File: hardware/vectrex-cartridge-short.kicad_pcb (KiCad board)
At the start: 2 copper layers, 48 x 66.1 mm, 18 parts, among them CON1 vectrex-edge-connector, SW2 SW_DIP_x03, U1 AT27C256R-70PU / AT27C512R-70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, U2 DS2431+ TO-92

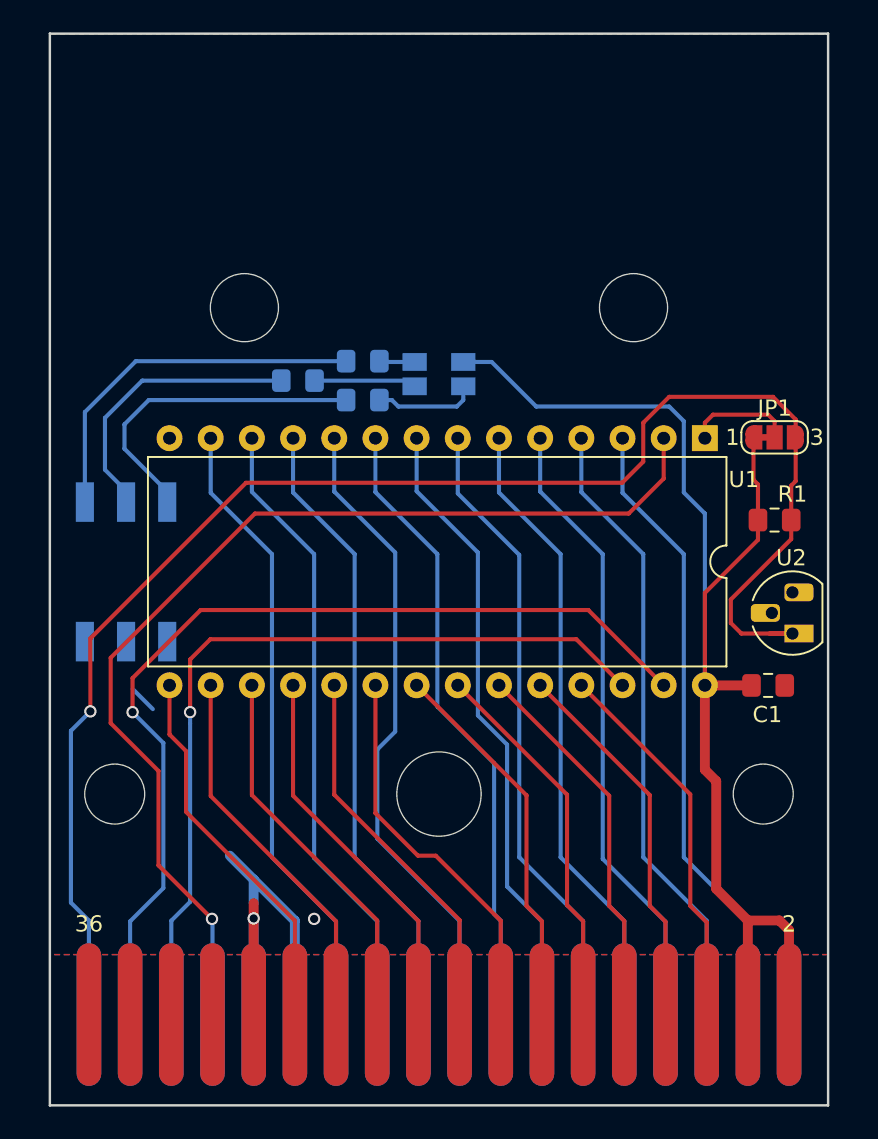
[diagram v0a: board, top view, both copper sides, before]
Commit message: added RGB LED to Vectrex Cartridge v1.1, also added stand-alone LED PCB v1.0
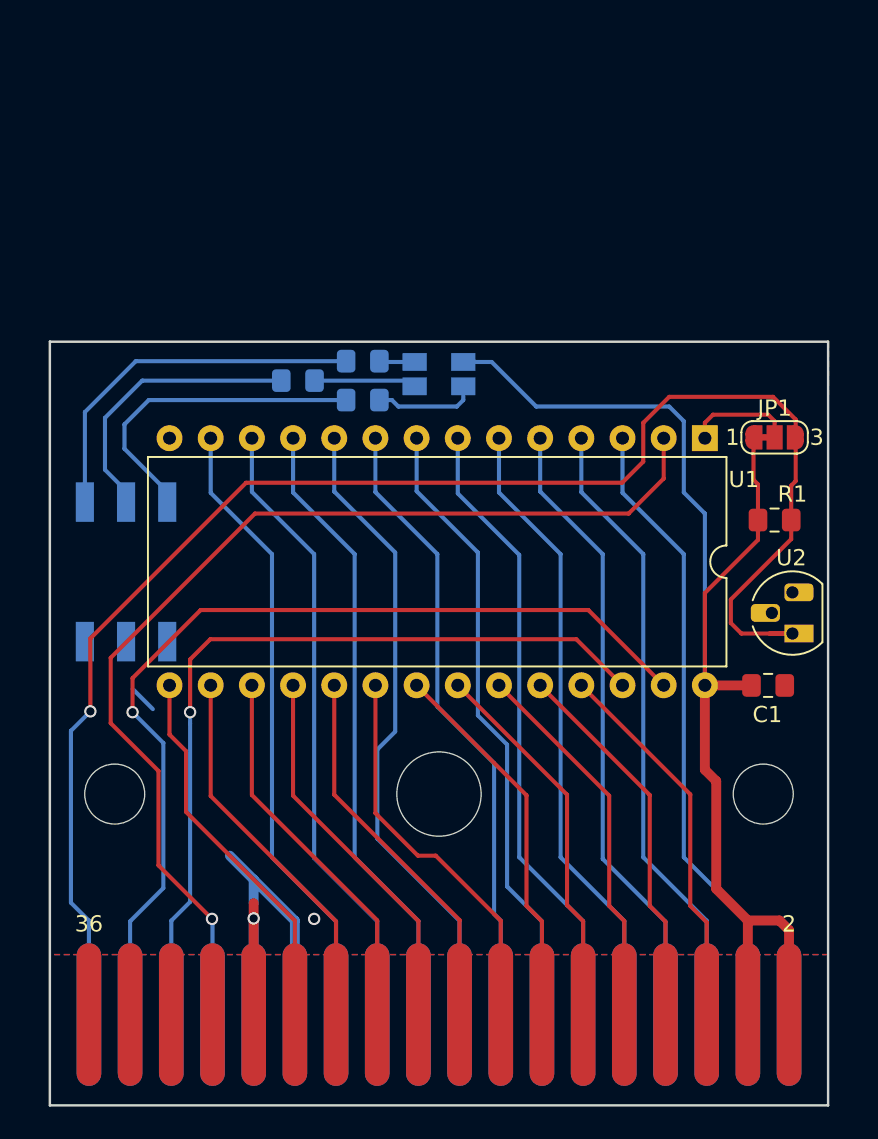
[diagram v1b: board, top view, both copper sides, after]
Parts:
- removed G3: LOGO, vectrex-cartridge:vectrex-uk-soldermask
- removed H4, H5: 4.2mm, vectrex-cartridge:Mounting_Hole_D4.2mm
- G1: footprint vectrex-cartridge:vectrex-us-soldermask -> vectrex-cartridge:vectrex-us-soldermask-37mm; moved to B.Cu
- moved G1 24.5 mm to (146.1, 101.9), turned to 180 degrees
- renumbered SW2 to SW1
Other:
- board size 48 x 66.1 mm -> 48 x 47.1 mm
- board text removed: "4.2mm hole"

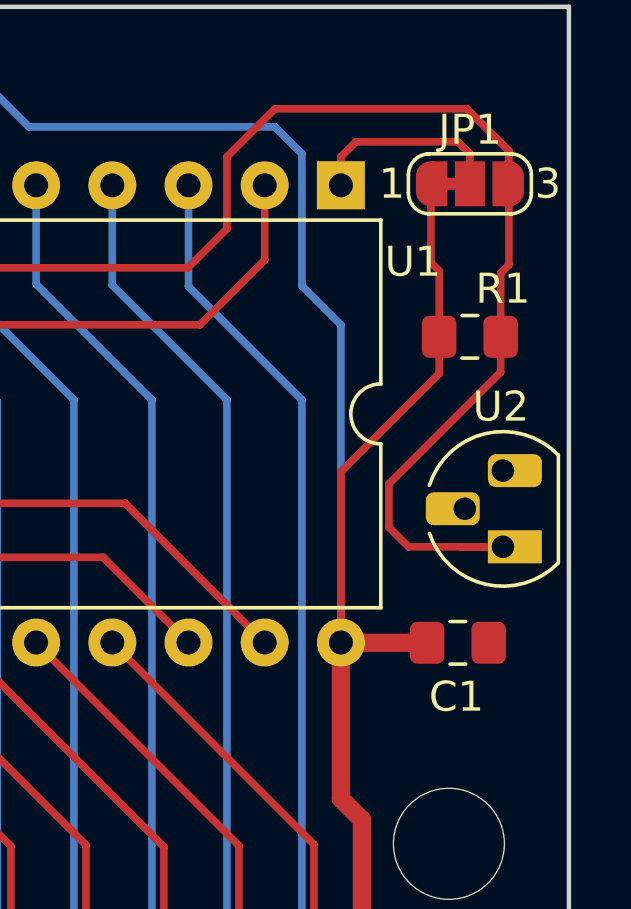
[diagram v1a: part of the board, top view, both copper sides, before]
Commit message: Updated DS2431 footprint, and many little tweaks for v1.2
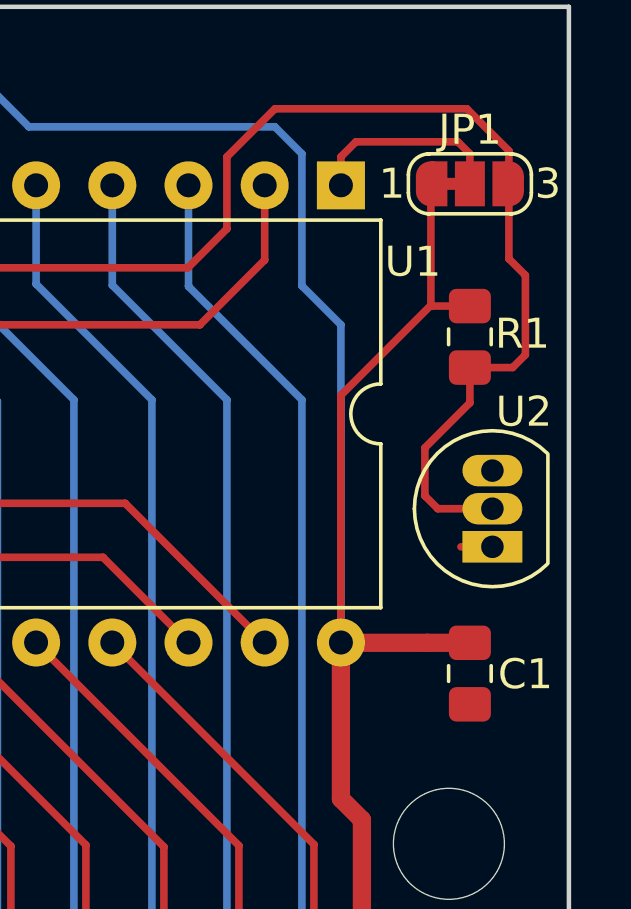
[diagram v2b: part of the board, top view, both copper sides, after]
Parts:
- added G2: LOGO, vectrex-cartridge:vectrex-us-soldermask-15mm, F.Cu at (141.7, 92.2)
- R2, R3: value 220 0805 -> 200 0805
- R4: value 150 0805 -> 120 0805
- U2: footprint vectrex-cartridge:TO-92L_HandSolder -> vectrex-cartridge:TO-92_Inline_BW
- moved C1 1.10 mm to (162.4, 111.9), turned to 270 degrees
- moved U2 0.35 mm to (163.2, 107.7)
- turned R1 to 270 degrees
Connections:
- U2 pad 1: V-PB6 -> GND
- U2 pad 2: GND -> V-PB6
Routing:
- net V-PB6: track 95.2 -> 92.2 mm
- net +5V: track 81.0 -> 83.5 mm
- net GND: track 27.5 -> 28.6 mm

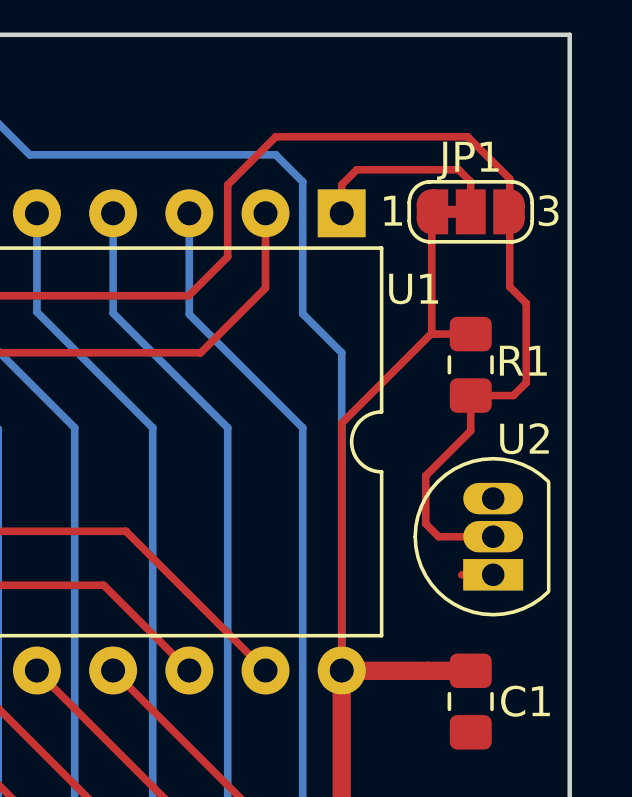
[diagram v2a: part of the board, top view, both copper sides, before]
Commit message: migrate 3D shapes to built-in KiCad 6.x location
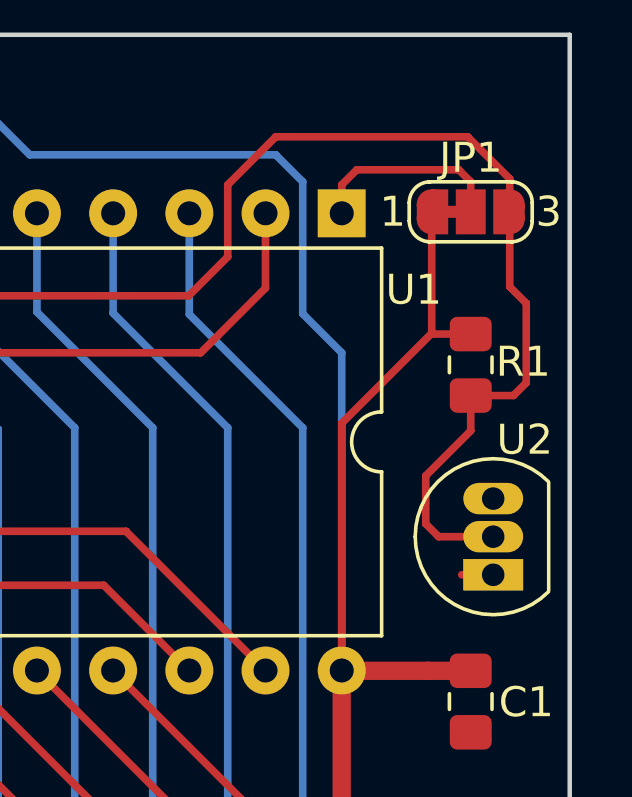
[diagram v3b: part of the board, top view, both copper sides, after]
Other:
- net class Default removed
- net class Large removed

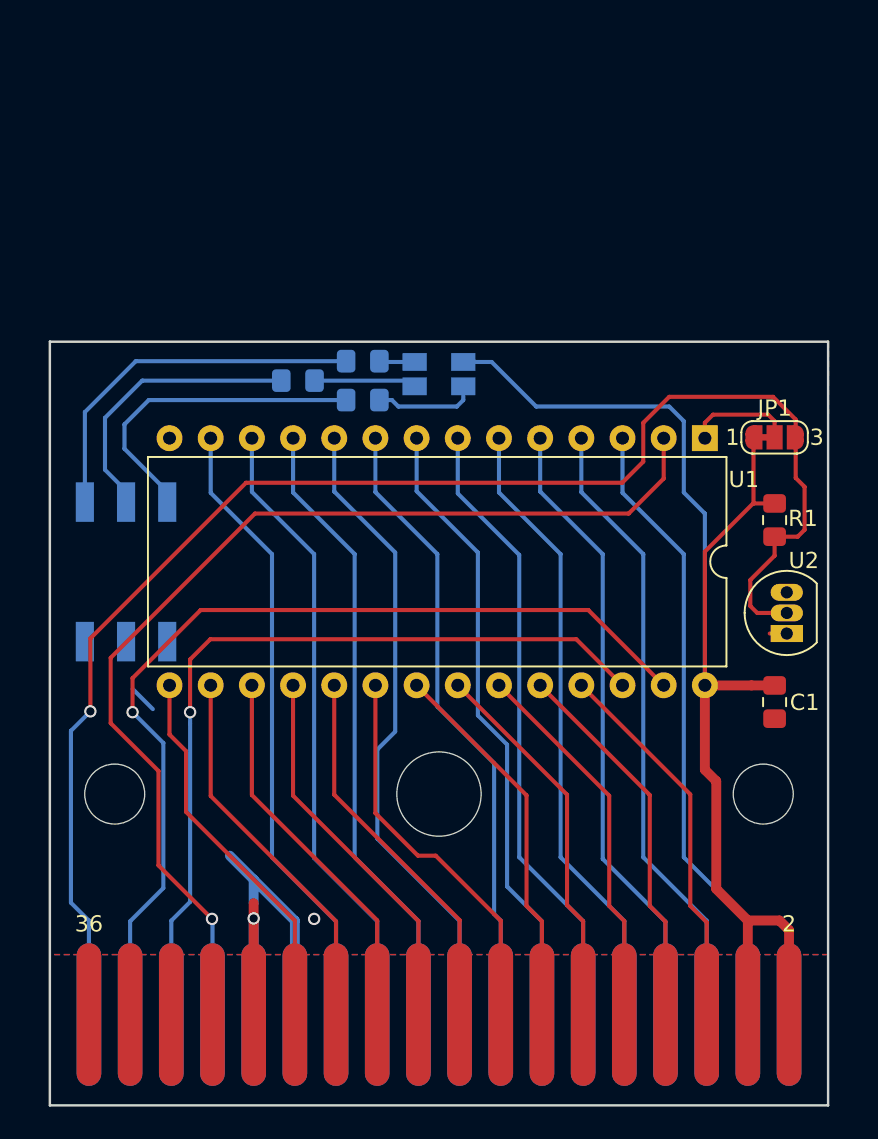
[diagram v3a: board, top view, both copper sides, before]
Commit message: update vectrex-cartridge-short to v1.4 all SMT
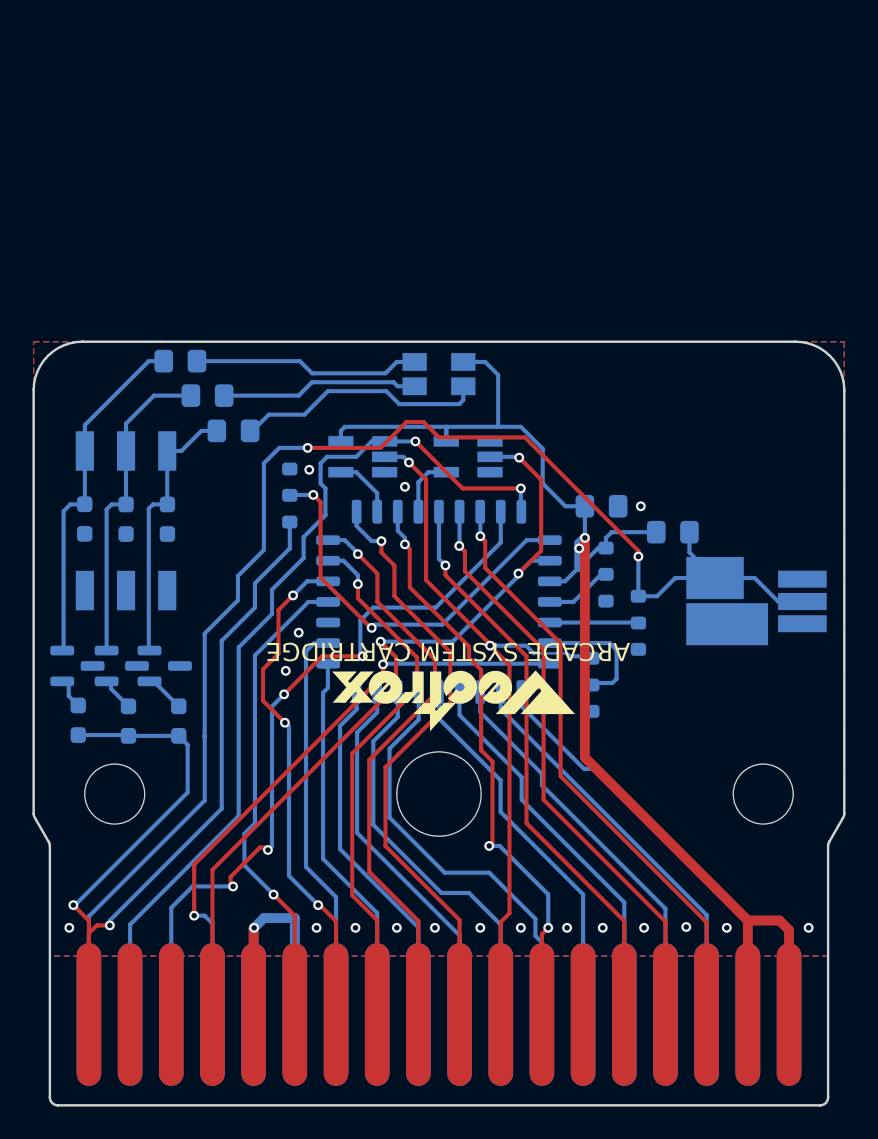
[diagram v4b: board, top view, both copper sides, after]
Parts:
- added JP2: PB6/A16/GND, vectrex-cartridge:R_0603_1608Metric_Jumper_12_Bridged, B.Cu at (154.0, 106.2)
- added JP3: IRQ/A17/GND, vectrex-cartridge:R_0603_1608Metric_Jumper_12_Bridged, B.Cu at (132.5, 100.0)
- added JP4: GND/A18/+5V, vectrex-cartridge:R_0603_1608Metric_Jumper_12_Bridged, B.Cu at (152.0, 104.9)
- added Q2: MMBT4403, Package_TO_SOT_SMD:SOT-23, B.Cu at (124.8, 109.7)
- added Q3: MMBT4403, Package_TO_SOT_SMD:SOT-23, B.Cu at (122.1, 109.7)
- added Q4: MMBT4403, Package_TO_SOT_SMD:SOT-23, B.Cu at (119.4, 109.7)
- added R12: 0 0603, Resistor_SMD:R_0603_1608Metric_Pad0.98x0.95mm_HandSolder, B.Cu at (125.0, 100.7)
- added R13: 0 0603, Resistor_SMD:R_0603_1608Metric_Pad0.98x0.95mm_HandSolder, B.Cu at (122.4, 100.7)
- added R14: 0 0603, Resistor_SMD:R_0603_1608Metric_Pad0.98x0.95mm_HandSolder, B.Cu at (119.8, 100.6)
- added R22: 1k 0603, Resistor_SMD:R_0603_1608Metric_Pad0.98x0.95mm_HandSolder, B.Cu at (125.7, 113.1)
- added R23: 1k 0603, Resistor_SMD:R_0603_1608Metric_Pad0.98x0.95mm_HandSolder, B.Cu at (122.5, 113.1)
- added R24: 1k 0603, Resistor_SMD:R_0603_1608Metric_Pad0.98x0.95mm_HandSolder, B.Cu at (119.5, 113.0)
- added U3: SN74AHC1G04DBVR (Schmitt-Trigger), Package_TO_SOT_SMD:SOT-23-5_HandSoldering, B.Cu at (143.5, 96.8)
- added U4: DS2431+ TO-92, vectrex-cartridge:TO-92_Inline_BW_SMT, B.Cu at (164.1, 107.0)
- added U5: DS2431G+ 2-SFN, vectrex-cartridge:2SFN_6mmx6mm, B.Cu at (159.2, 105.7)
- C1, R1: moved to B.Cu
- CON1: footprint vectrex-cartridge:vectrex-edge-connector-thinner-no-soldermask -> vectrex-cartridge:vectrex-edge-connector-thinner-no-soldermask-no-silk
- G1: footprint vectrex-cartridge:vectrex-us-soldermask-37mm -> vectrex-cartridge:vectrex-us-soldermask-15mm
- G2: footprint vectrex-cartridge:vectrex-us-soldermask-15mm -> vectrex-cartridge:vectrex-us-silkscreen-15mm
- JP1: value SolderJumper_3_Bridged12 -> C_A15/A15/GND; footprint vectrex-cartridge:SolderJumper-3_P1.3mm_Bridged12_RoundedPad1.0x1.5mm_NumberLabels -> vectrex-cartridge:R_0603_1608Metric_Jumper_12_Bridged; moved to B.Cu
- R2, R3: value 200 0805 -> 150 0805
- R4: value 120 0805 -> 200 0805
- SW1: footprint Button_Switch_SMD:SW_DIP_SPSTx03_Slide_6.7x9.18mm_W8.61mm_P2.54mm_LowProfile -> vectrex-cartridge:SW_DIP_SPSTx03_Slide_6.7x9.18mm_W8.61mm_P2.54mm_LowProfile_NoSWSilk
- U1: value AT27C256R-70PU / AT27C512R-70PU -> SST39SF010A/020A/040A; footprint Package_DIP:DIP-28_W15.24mm -> Package_LCC:PLCC-32_11.4x14.0mm_P1.27mm; moved to B.Cu
- U2: value DS2431+ TO-92 -> NC7ST08M5X (Do Not Substitute); footprint vectrex-cartridge:TO-92_Inline_BW -> Package_TO_SOT_SMD:SOT-23-5_HandSoldering; moved to B.Cu
- moved U2 28.3 mm to (137.0, 96.8), turned to 180 degrees
- moved G2 19.6 mm to (142.6, 111.8), turned to 180 degrees
- moved U1 19.3 mm to (141.7, 105.8), turned to 90 degrees
- moved JP1 18.3 mm to (151.1, 110.0), turned to -90 degrees
- moved C1 16.1 mm to (151.7, 99.8), turned to 0 degrees
- moved G1 14.1 mm to (157.2, 93.2)
- moved R4 11.2 mm to (125.8, 90.9)
- moved R2 8.20 mm to (129.0, 95.2)
- moved R1 6.32 mm to (156.1, 101.5), turned to 0 degrees
- moved R3 5.65 mm to (127.4, 93.0)
- moved SW1 3.15 mm to (122.4, 100.7)
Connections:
- CON1 pad 16: V-CE -> C_A15
- JP1 pad 1: +5V -> C_A15
- JP1 pad 2: Net-(JP1-Pad2) -> Net-(JP1-C)
- JP1 pad 3: V-PB6 -> GND
- U1 pad 1: Net-(JP1-Pad2) -> Net-(JP4-C)
- U1 pad 10: C_A0 -> C_A2
- U1 pad 11: C_D0 -> C_A1
- U1 pad 12: C_D1 -> C_A0
- U1 pad 13: C_D2 -> C_D0
- U1 pad 14: GND -> C_D1
- U1 pad 15: C_D3 -> C_D2
- U1 pad 16: C_D4 -> GND
- U1 pad 17: C_D5 -> C_D3
- U1 pad 18: C_D6 -> C_D4
- U1 pad 19: C_D7 -> C_D5
- U1 pad 2: C_A12 -> Net-(JP2-C)
- U1 pad 20: V-CE -> C_D6
- U1 pad 21: C_A10 -> C_D7
- U1 pad 22: V-OE -> C000_FFFF
- U1 pad 23: C_A11 -> C_A10
- U1 pad 24: C_A9 -> /V-RW
- U1 pad 25: C_A8 -> C_A11
- U1 pad 26: C_A13 -> C_A9
- U1 pad 27: C_A14 -> C_A8
- U1 pad 28: +5V -> C_A13
- U1 pad 3: C_A7 -> Net-(JP1-C)
- U1 pad 4: C_A6 -> C_A12
- U1 pad 5: C_A5 -> C_A7
- U1 pad 6: C_A4 -> C_A6
- U1 pad 7: C_A3 -> C_A5
- U1 pad 8: C_A2 -> C_A4
- U1 pad 9: C_A1 -> C_A3
- U2 pad 1: GND -> C_A14
- U2 pad 2: V-PB6 -> C_A15
- U2 pad 3: (no net) -> GND
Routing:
- net V-IRQ: track 0.00 -> 63.0 mm, vias 0 -> 2
- net V-RW: track 0.00 -> 50.8 mm, vias 0 -> 3
- net C_A15: track 0.00 -> 45.3 mm, vias 0 -> 2
- net C_A12: track 65.8 -> 37.6 mm, vias 1 -> 2
- net Net-(JP3-C): track 0.00 -> 24.4 mm, vias 0 -> 2
- net V-CE: track 24.1 -> 0.00 mm
- net V-OE: track 23.5 -> 0.00 mm
- net C_A0: track 39.7 -> 23.0 mm
- net C_D0: track 38.7 -> 22.3 mm
- net C_D1: track 38.7 -> 23.5 mm
- net C_A3: track 38.7 -> 23.6 mm
- net C_A4: track 38.7 -> 24.1 mm
- net C_A5: track 38.7 -> 24.6 mm
- net C_D2: track 38.7 -> 24.7 mm
- net C_A1: track 38.7 -> 24.8 mm
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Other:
- board size 48 x 47.1 mm -> 50 x 47.1 mm
- board text added: "0.1uf"
- board text added: "04"
- board text added: "08"
- board text added: "1 2 3"
- board text added: "150"
- board text added: "200"
- board text added: "3 2 1"
- board text added: "3.3k"
- board text added: "ARCADE SYSTEM CARTRIDGE"
- board text added: "BAW"
- board text added: "IRQ|A17|GND"
- board text added: "JP1:A15|A15|GND JP2:PB6|A16|GND JP3: JP4:GND|A18|VCC"
- board text added: "THIS SIDE DOWN!"
- board text added: "v1.4"
- board text removed: "3.7mm hole"
- board text removed: "5.2mm hole"
